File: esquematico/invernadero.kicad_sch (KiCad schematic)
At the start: 19 parts, among them J1 Toma 110V AC, K1 Modulo rele 5V (SRD-05VDC), M1 Bomba de riego 110V, U1 Raspberry Pi 5 (GPIO 40 pines), U2 MCP3008 (ADC SPI), U3 DHT-11 Temp/Hum, U4 TMP36 Temp, U5 Sensor agua S8050 (lluvia), U6 FC-28 Humedad suelo, U7 HC-SR04 Nivel tanque

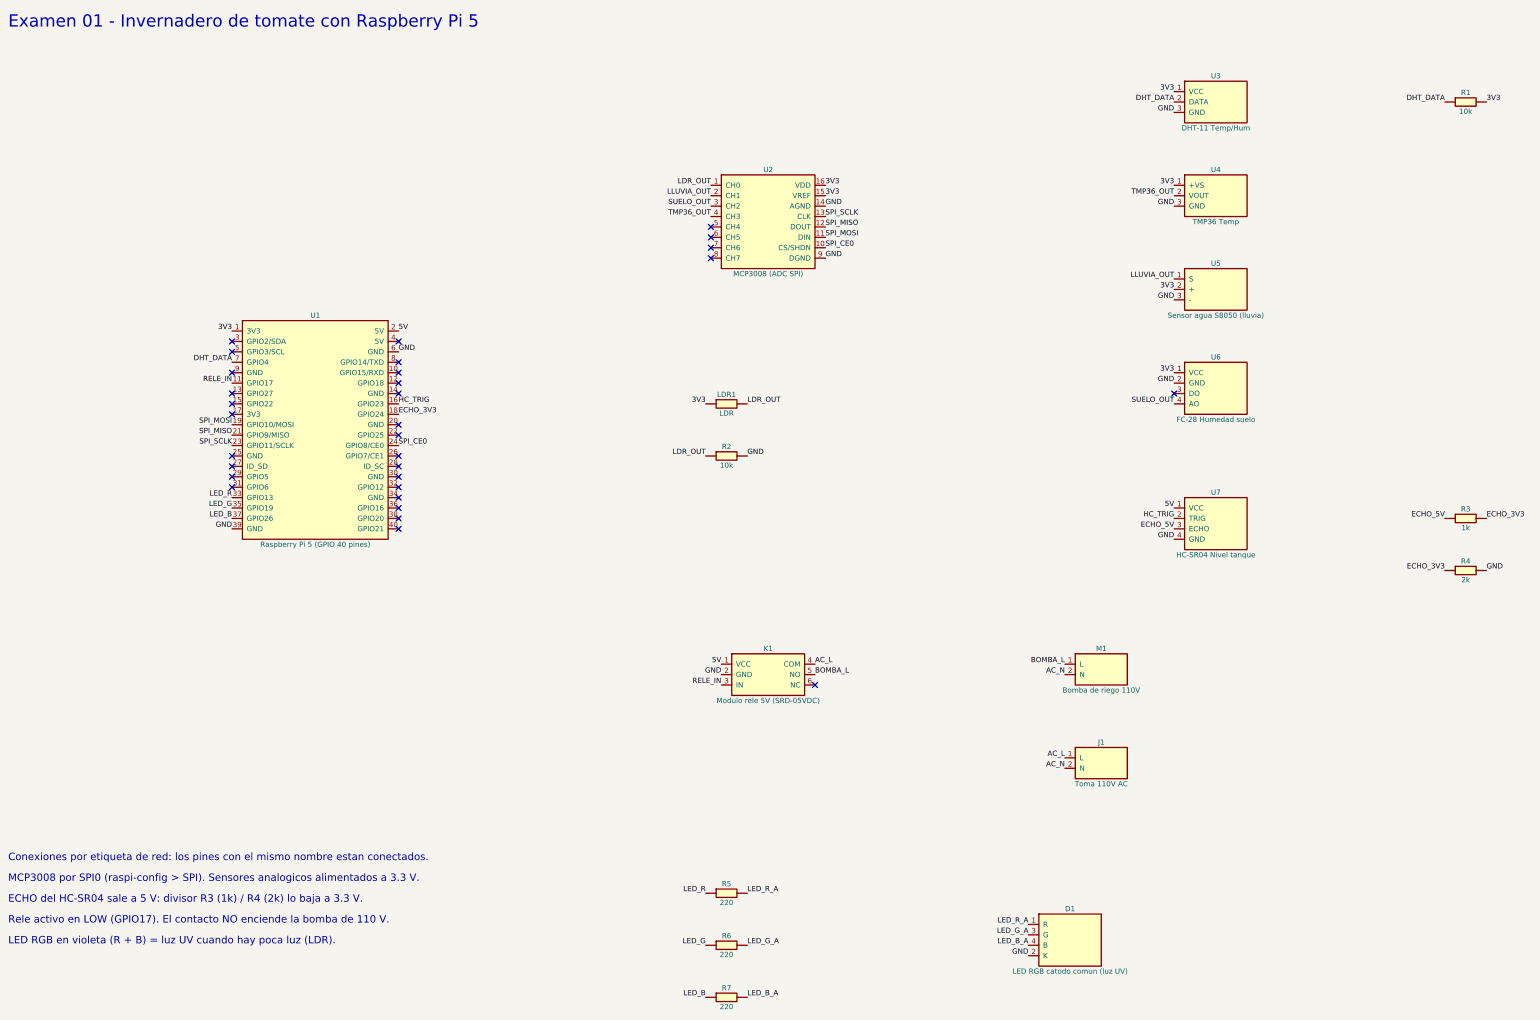
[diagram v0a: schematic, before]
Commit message: Ítem 7: esquemático actualizado al armado actual y exportado a PNG
Sin MCP3008 ni relé, todos los sensores a 3V3 y los mismos GPIO del código.

Co-Authored-By: Claude Opus 5.5 <noreply@anthropic.com>
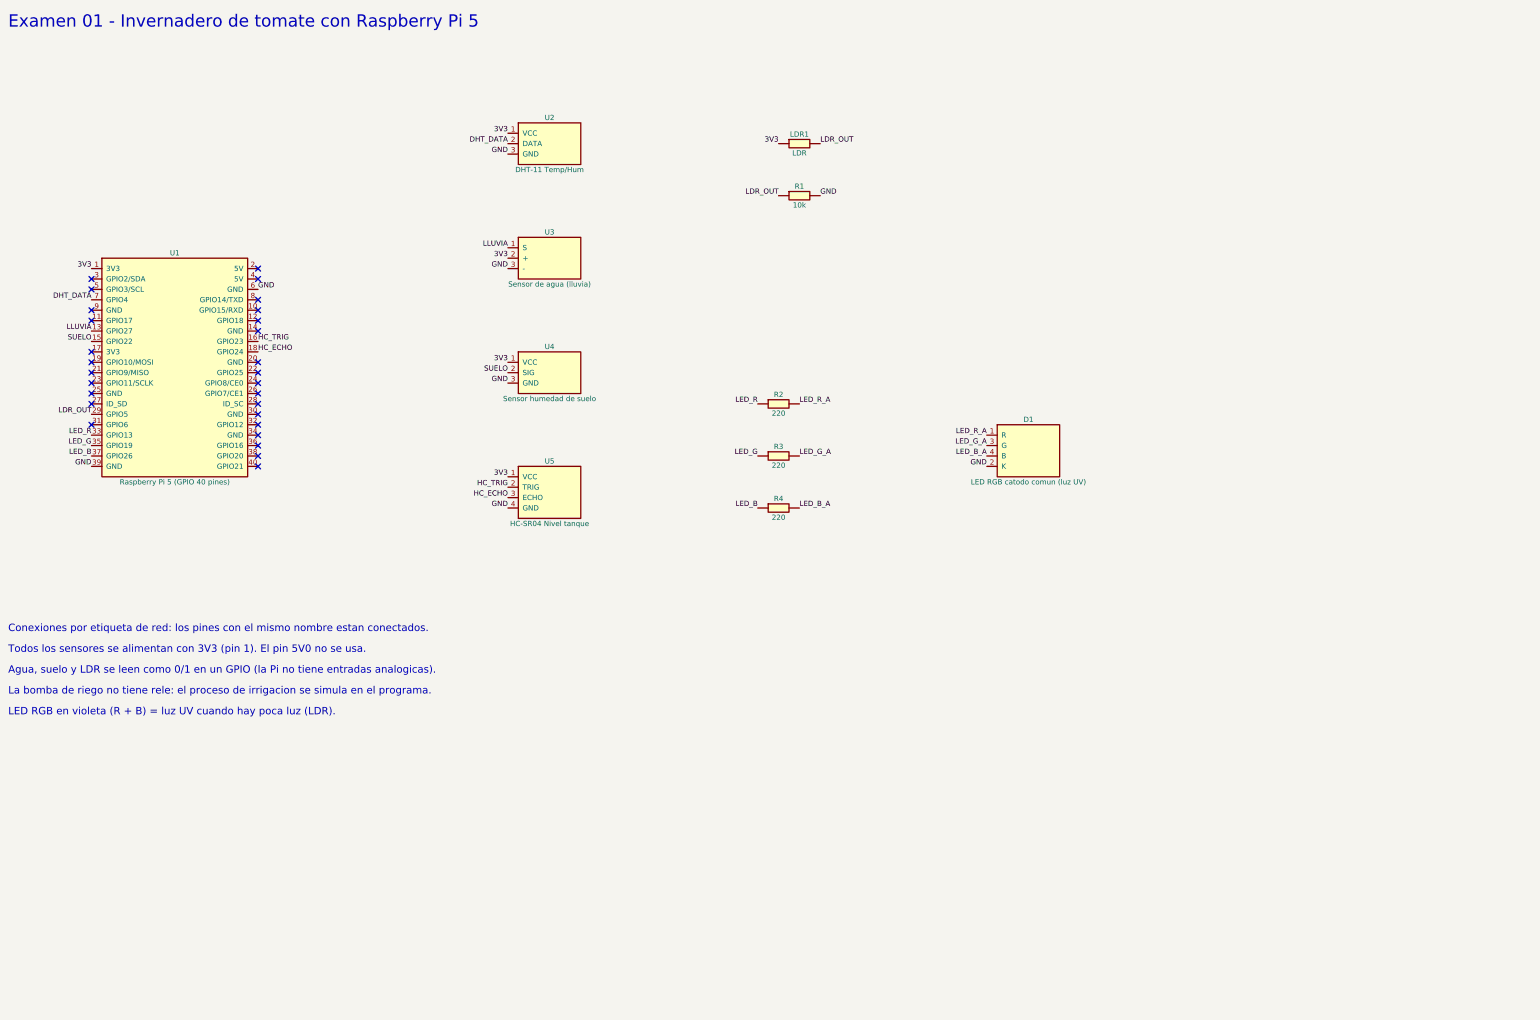
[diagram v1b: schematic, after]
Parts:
- removed J1: Toma 110V AC, symbol inv:AC
- removed K1: Modulo rele 5V (SRD-05VDC), symbol inv:RELE
- removed M1: Bomba de riego 110V, symbol inv:BOMBA
- removed R5, R6, R7: 220, symbol inv:R
- removed U2: MCP3008 (ADC SPI), symbol inv:MCP3008
- removed U3: DHT-11 Temp/Hum, symbol inv:DHT11
- removed U4: TMP36 Temp, symbol inv:TMP36
- removed U5: Sensor agua S8050 (lluvia), symbol inv:LLUVIA
- removed U6: FC-28 Humedad suelo, symbol inv:FC28
- removed U7: HC-SR04 Nivel tanque, symbol inv:HCSR04
- added U2: DHT-11 Temp/Hum, symbol inv:DHT11
- added U3: Sensor de agua (lluvia), symbol inv:LLUVIA
- added U4: Sensor humedad de suelo, symbol inv:SUELO
- added U5: HC-SR04 Nivel tanque, symbol inv:HCSR04
- R2: value 10k -> 220
- R3: value 1k -> 220
- R4: value 2k -> 220
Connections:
- net ECHO_5V is gone; now on net LED_G: R3.1
- net 3V3: now also U2.1 (VCC), U3.2 (+), U4.1 (VCC), U5.1 (VCC); no longer R1.2
- net DHT_DATA: now also U2.2 (DATA); no longer R1.1
- net GND: now also R1.2, U2.3 (GND), U3.3 (-), U4.3 (GND), U5.4 (GND); no longer R2.2, R4.2
- net HC_TRIG: now also U5.2 (TRIG)
- net LDR_OUT: now also R1.1, U1.29 (GPIO5); no longer R2.1
- net LED_B: now also R4.1
- net LED_B_A: now also R4.2
- net LED_G_A: now also R3.2
- net LED_R: now also R2.1
- net LED_R_A: now also R2.2
- net LLUVIA: now reaches U1.13 (GPIO27)
- net LLUVIA: now also U3.1 (S)
- net SUELO: now reaches U1.15 (GPIO22)
- net SUELO: now also U4.2 (SIG)
- net 5V: no longer names the net of U1.2 (5V)
- removed net ECHO_3V3: R3.2, R4.1, U1.18 (GPIO24)
- net RELE_IN: no longer names the net of U1.11 (GPIO17)
- net SPI_CE0: no longer names the net of U1.24 (GPIO8/CE0)
- net SPI_MISO: no longer names the net of U1.21 (GPIO9/MISO)
- net SPI_MOSI: no longer names the net of U1.19 (GPIO10/MOSI)
- net SPI_SCLK: no longer names the net of U1.23 (GPIO11/SCLK)
- new net HC_ECHO: U1.18 (GPIO24), U5.3 (ECHO)
- no-connect marks 31 -> 28
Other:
- note added: "Agua, suelo y LDR se leen como 0/1 en un GPIO (la Pi no tiene entradas analogicas)."
- note added: "La bomba de riego no tiene rele: el proceso de irrigacion se simula en el programa."
- note added: "Todos los sensores se alimentan con 3V3 (pin 1). El pin 5V0 no se usa."
- note removed: "ECHO del HC-SR04 sale a 5 V: divisor R3 (1k) / R4 (2k) lo baja a 3.3 V."
- note removed: "MCP3008 por SPI0 (raspi-config > SPI). Sensores analogicos alimentados a 3.3 V."
- note removed: "Rele activo en LOW (GPIO17). El contacto NO enciende la bomba de 110 V."
